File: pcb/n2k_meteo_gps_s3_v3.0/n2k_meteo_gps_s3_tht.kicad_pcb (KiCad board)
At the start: 2 copper layers, 59 x 74.8 mm, 45 parts, among them U1 MCP2562-E-P, U2 ESP32-S3_SUPERMINI, U3 PC817, U4 74AHC1G14, U5 TSR_1-2450, U6 TSR1-2433E

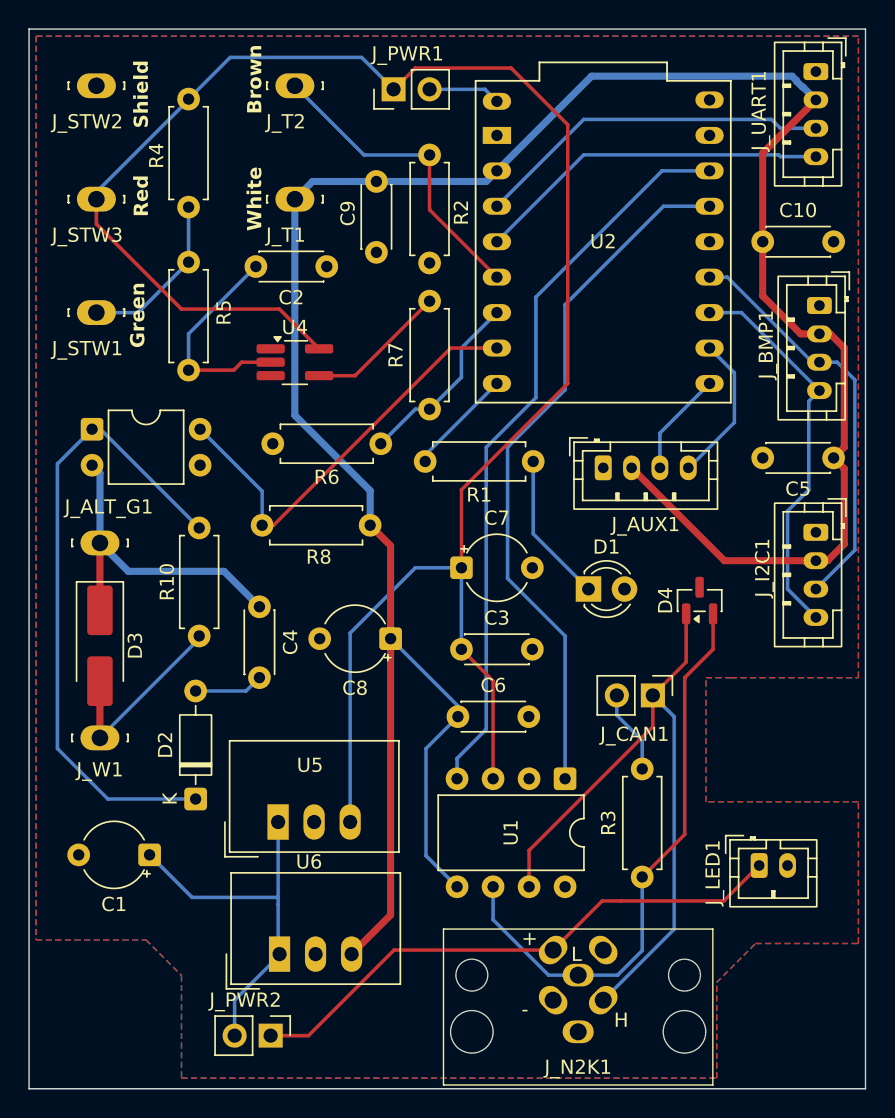
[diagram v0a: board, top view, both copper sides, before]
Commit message: clean up old unused pcb and configurations
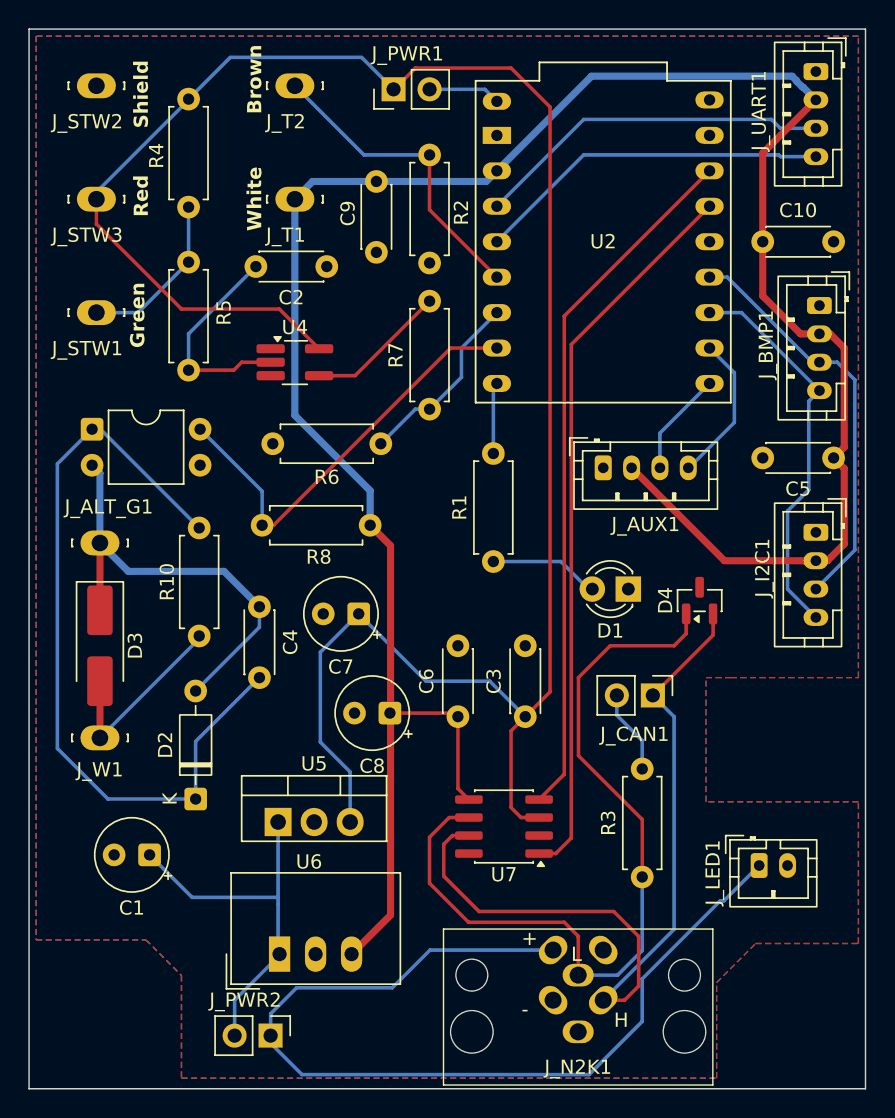
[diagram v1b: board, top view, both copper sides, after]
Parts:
- removed U1: MCP2562-E-P, Package_DIP:DIP-8_W7.62mm
- added U7: MCP2562-E-SN, Package_SO:SOIC-8_3.9x4.9mm_P1.27mm, F.Cu at (49.0, 76.5)
- C1, C7, C8: footprint Capacitor_THT:CP_Radial_Tantal_D4.5mm_P5.00mm -> Capacitor_THT:CP_Radial_Tantal_D5.0mm_P2.50mm
- C4: value 100nF -> 10nF
- R1: value 100Ω -> 220Ω
- R6: value 12K -> 10K
- U5: value TSR_1-2450 -> LM7805_TO220; footprint Converter_DCDC:Converter_DCDC_TRACO_TSR-1_THT -> Package_TO_SOT_THT:TO-220-3_Vertical
- moved C7 7.95 mm to (38.8, 61.5), turned to 180 degrees
- moved R1 7.60 mm to (48.3, 57.8), turned to 90 degrees
- moved C3 6.54 mm to (50.5, 68.8), turned to 90 degrees
- moved C8 5.25 mm to (41.0, 68.5)
- moved D1 2.81 mm to (57.8, 59.8), turned to 180 degrees
- turned C6 to 90 degrees
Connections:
- C4 pad 1: Net-(D3-A1) -> Net-(D2-A)
- C4 pad 2: Net-(D2-A) -> Net-(D2-K)
- D1 pad 1: Net-(D1-K) -> GND
- D1 pad 2: GND -> Net-(D1-A)
- D3 pad 1: Net-(D3-A1) -> Net-(D2-A)
- D4 pad 1: Net-(J_CAN1-Pin_1) -> Net-(J_N2K1-Pin_1)
- D4 pad 2: Net-(J_N2K1-Pin_1) -> Net-(J_CAN1-Pin_1)
- J_ALT_G1 pad 1: Net-(D3-A1) -> Net-(D2-A)
- R1 pad 1: Net-(D1-K) -> Net-(D1-A)
- U3 pad 2: Net-(D3-A1) -> Net-(D2-A)
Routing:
- net Net-(J_LED1-Pin_1): track 39.4 -> 67.1 mm
- net Net-(D2-A): track 4.89 -> 31.9 mm
- net Net-(D3-A1): track 24.1 -> 0.00 mm
- net Net-(J_N2K1-Pin_1): track 41.0 -> 58.0 mm
- net Net-(D1-K): track 10.6 -> 0.00 mm
- net Net-(D2-K): track 45.2 -> 55.6 mm
- net +3.3V: track 175.7 -> 165.5 mm
- net Net-(J_CAN1-Pin_1): track 48.1 -> 57.9 mm
- net +5V: track 135.3 -> 144.5 mm
- net Net-(D1-A): track 0.00 -> 7.51 mm
- net Net-(U2-GPIO13): track 52.2 -> 49.3 mm
- net Net-(U2-GPIO6): track 7.60 -> 5.04 mm
- net Net-(U2-GPIO12): track 49.9 -> 51.3 mm

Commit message: Added ability to change the passkey
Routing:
- net Net-(J_UART1-Pin_3): track 25.3 -> 24.8 mm
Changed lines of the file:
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@@
+	)
+	(segment
+		(start 48.55 32.75)
+		(end 52.3 29)
+		(width 0.25)
+		(layer "B.Cu")
+		(net 8)
+	)
+	(segment
+		(start 52.3 29)
+		(end 66.8 29)
+		(width 0.25)
+		(layer "B.Cu")
+		(net 8)
+	)
+	(segment
+		(start 66.8 29)
+		(end 68.55 27.25)
+		(width 0.25)
+		(layer "B.Cu")
+		(net 8)
 	)
 	(segment
@@
 	)
 	(segment
-		(start 67.925 26.625)
-		(end 68.55 27.25)
-		(width 0.25)
-		(layer "B.Cu")
-		(net 8)
-	)
-	(segment
-		(start 54.675 26.625)
-		(end 67.925 26.625)
-		(width 0.25)
-		(layer "B.Cu")
-		(net 8)
-	)
-	(segment
-		(start 48.55 32.75)
-		(end 54.675 26.625)
-		(width 0.25)
-		(layer "B.Cu")
-		(net 8)
-	)
-	(segment
 		(start 48.3 45.5)
 		(end 48.3 50.19)
@@
 	)
 	(segment
+		(start 48.55 35.25)
+		(end 52.3 31.5)
+		(width 0.25)
+		(layer "B.Cu")
+		(net 12)
+	)
+	(segment
+		(start 66.3 31.5)
+		(end 68.55 29.25)
+		(width 0.25)
+		(layer "B.Cu")
+		(net 12)
+	)
+	(segment
 		(start 68.55 29.25)
 		(end 71.05 29.25)
@@
 	)
 	(segment
-		(start 68.425 29.125)
-		(end 68.55 29.25)
-		(width 0.25)
-		(layer "B.Cu")
-		(net 12)
-	)
-	(segment
-		(start 54.675 29.125)
-		(end 68.425 29.125)
-		(width 0.25)
-		(layer "B.Cu")
-		(net 12)
-	)
-	(segment
-		(start 48.55 35.25)
-		(end 54.675 29.125)
-		(width 0.25)
-		(layer "B.Cu")
+		(start 52.3 31.5)
+		(end 66.3 31.5)
+		(width 0.25)
+		(layer "B.Cu")
